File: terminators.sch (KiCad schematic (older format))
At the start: 12 parts

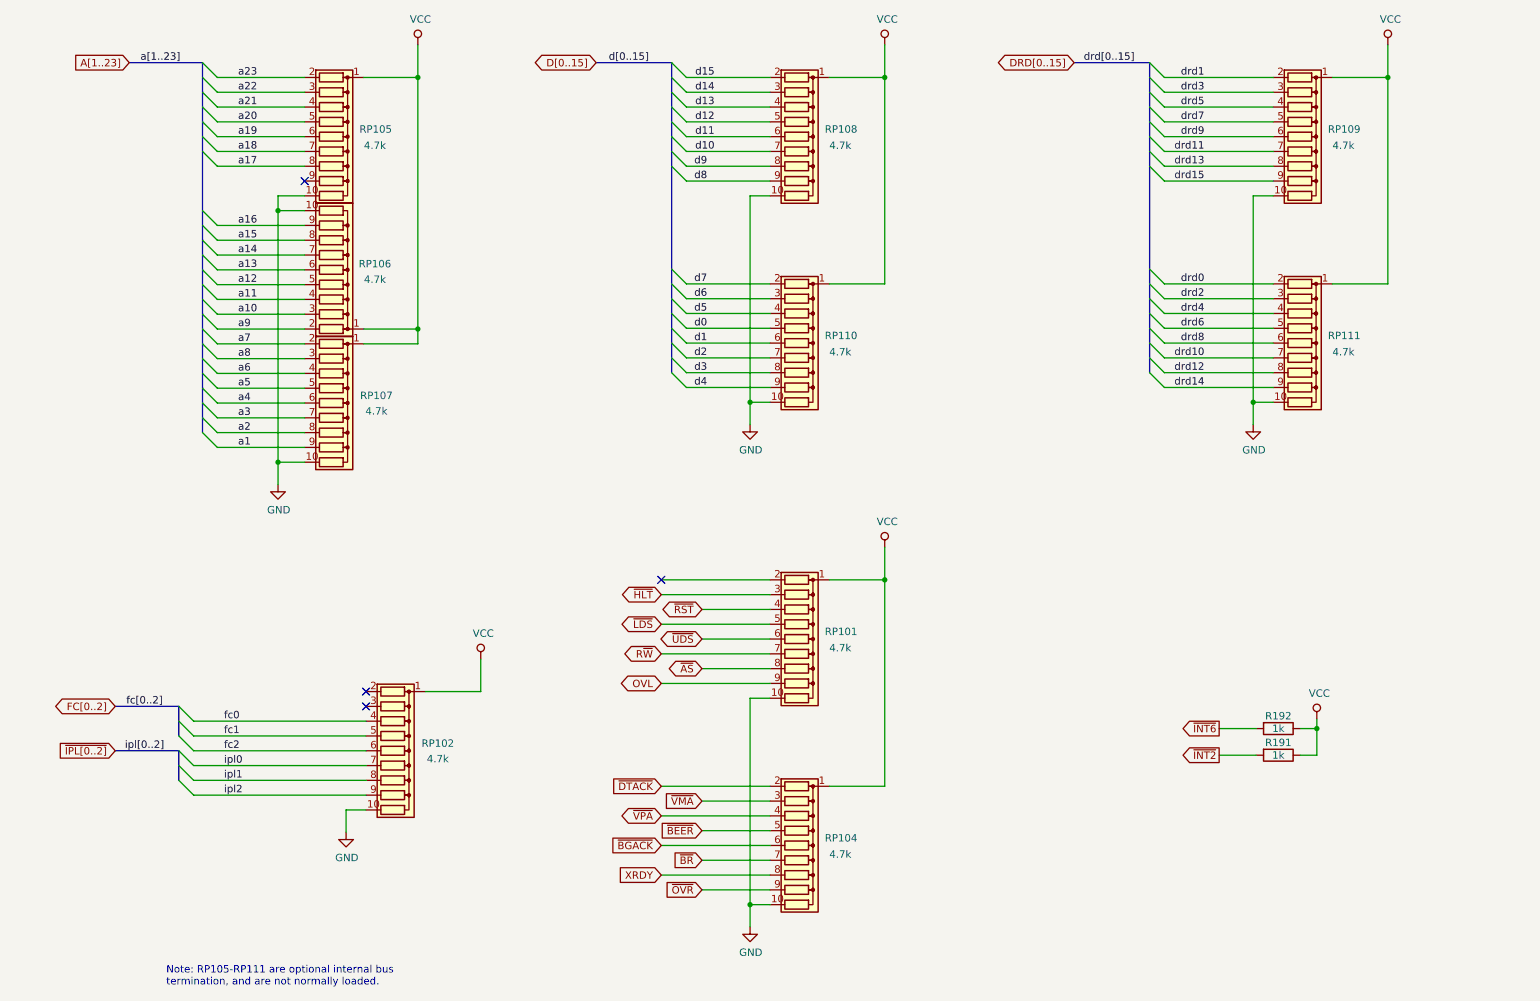
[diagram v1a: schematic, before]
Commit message: Add expansion bus
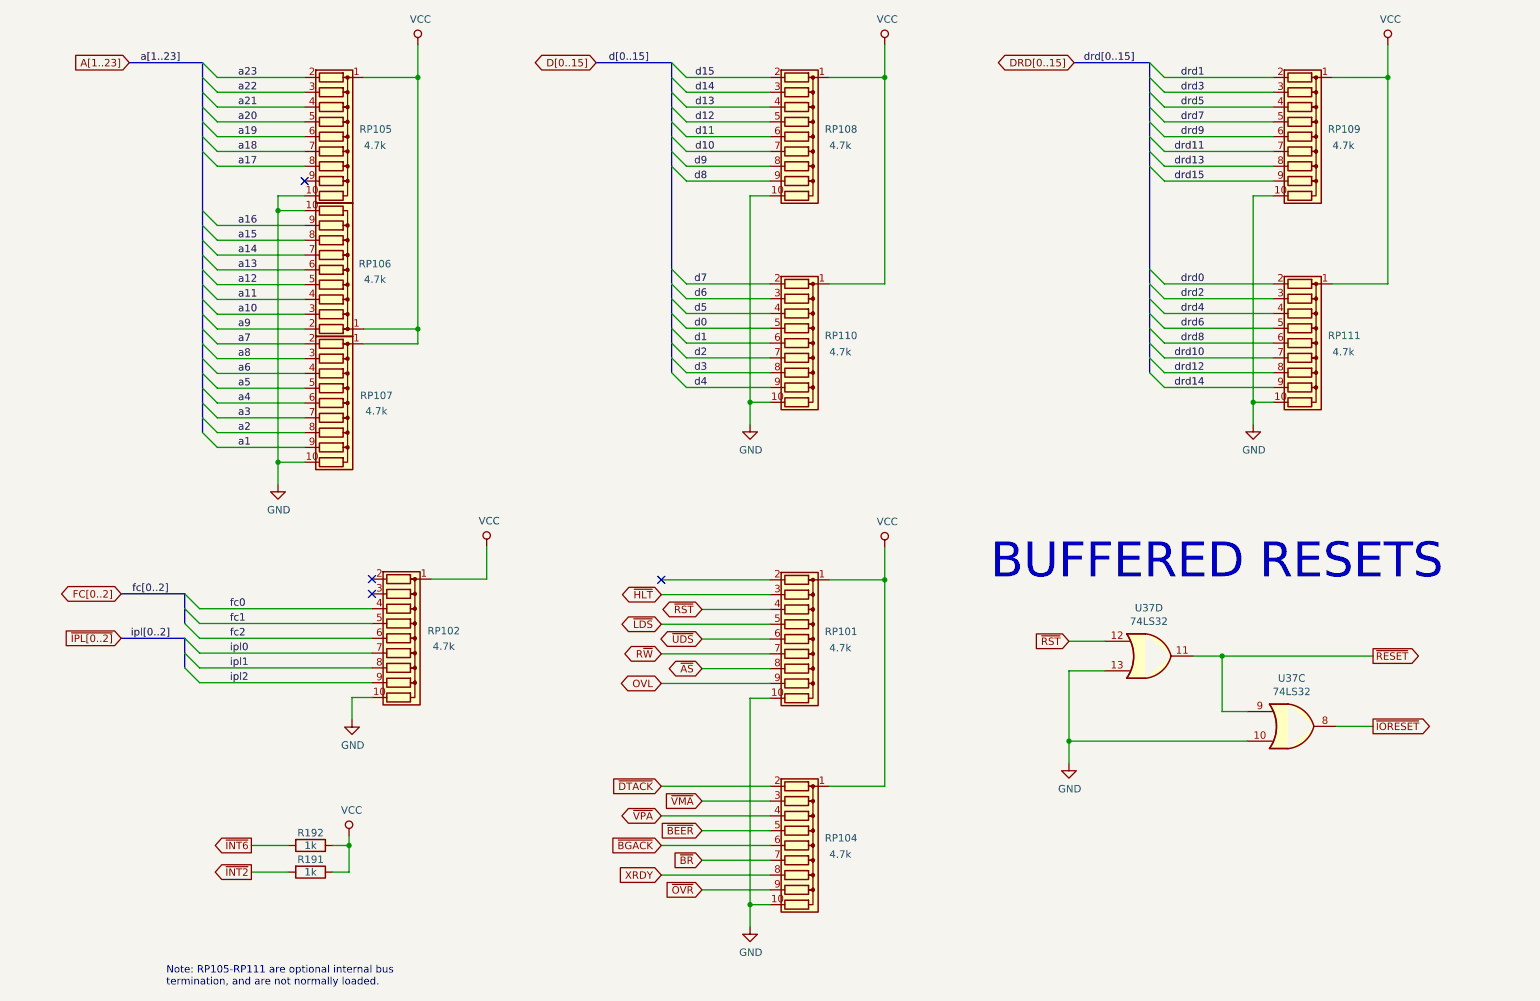
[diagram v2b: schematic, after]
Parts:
- added U37: 74LS32, symbol 74xx:74LS32
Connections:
- net GND: now also U37.10, U37.13
- net ~RST: now also U37.12
- new net ~IORESET: U37.8
- new net ~RESET: U37.11, U37.9
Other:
- note added: "BUFFERED RESETS"
- moved on the sheet: R191, R192, RP102
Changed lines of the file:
@@
 $Descr A4 11693 8268
 encoding utf-8
-Sheet 8 10
+Sheet 8 11
 Title "Rämixx500"
 Date "2019-04-20"
@@
 drd[0..15]
 Wire Wire Line
-	3370 5945 2205 5945
-Wire Wire Line
-	3370 6045 2205 6045
-Wire Wire Line
-	3370 6145 2205 6145
-Wire Wire Line
-	3370 5645 2205 5645
-Wire Wire Line
-	3370 5745 2205 5745
-Wire Wire Line
-	3370 5845 2205 5845
-Entry Wire Line
-	2105 5845 2205 5945
-Entry Wire Line
-	2105 5945 2205 6045
-Entry Wire Line
-	2105 6045 2205 6145
-Entry Wire Line
-	2105 5545 2205 5645
-Entry Wire Line
-	2105 5645 2205 5745
-Entry Wire Line
-	2105 5745 2205 5845
-Text GLabel 1675 5845 0    50   Input ~ 0
+	3410 5185 2245 5185
+Wire Wire Line
+	3410 5285 2245 5285
+Wire Wire Line
+	3410 5385 2245 5385
+Wire Wire Line
+	3410 4885 2245 4885
+Wire Wire Line
+	3410 4985 2245 4985
+Wire Wire Line
+	3410 5085 2245 5085
+Entry Wire Line
+	2145 5085 2245 5185
+Entry Wire Line
+	2145 5185 2245 5285
+Entry Wire Line
+	2145 5285 2245 5385
+Entry Wire Line
+	2145 4785 2245 4885
+Entry Wire Line
+	2145 4885 2245 4985
+Entry Wire Line
+	2145 4985 2245 5085
+Text GLabel 1715 5085 0    50   Input ~ 0
 ~IPL[0..2]
-Text GLabel 1675 5545 0    50   BiDi ~ 0
+Text GLabel 1715 4785 0    50   BiDi ~ 0
 FC[0..2]
-Text Label 1740 5845 0    50   ~ 0
+Text Label 1780 5085 0    50   ~ 0
 ipl[0..2]
-Text Label 1750 5545 0    50   ~ 0
+Text Label 1790 4785 0    50   ~ 0
 fc[0..2]
-Text Label 2410 5945 0    50   ~ 0
+Text Label 2450 5185 0    50   ~ 0
 ipl0
-Text Label 2410 6045 0    50   ~ 0
+Text Label 2450 5285 0    50   ~ 0
 ipl1
-Text Label 2410 6145 0    50   ~ 0
+Text Label 2450 5385 0    50   ~ 0
 ipl2
-Text Label 2410 5645 0    50   ~ 0
+Text Label 2450 4885 0    50   ~ 0
 fc0
-Text Label 2410 5745 0    50   ~ 0
+Text Label 2450 4985 0    50   ~ 0
 fc1
-Text Label 2410 5845 0    50   ~ 0
+Text Label 2450 5085 0    50   ~ 0
 fc2
 $Comp
 L Device:R_Network09 RP102
 U 1 1 5D7152A6
-P 3570 5845
-F 0 "RP102" V 3520 6130 50  0000 C CNN
-F 1 "4.7k" V 3625 6130 50  0000 C CNN
-F 2 "Resistor_THT:R_Array_SIP10" V 4145 5845 50  0001 C CNN
-F 3 "http://www.vishay.com/docs/31509/csc.pdf" H 3570 5845 50  0001 C CNN
-	1    3570 5845
-	0    1    1    0
-$EndComp
-NoConn ~ 3370 5445
-NoConn ~ 3370 5545
-Wire Wire Line
-	4145 5445 3770 5445
+P 3610 5085
+F 0 "RP102" V 3560 5370 50  0000 C CNN
+F 1 "4.7k" V 3665 5370 50  0000 C CNN
+F 2 "Resistor_THT:R_Array_SIP10" V 4185 5085 50  0001 C CNN
+F 3 "http://www.vishay.com/docs/31509/csc.pdf" H 3610 5085 50  0001 C CNN
+	1    3610 5085
+	0    1    1    0
+$EndComp
+NoConn ~ 3410 4685
+NoConn ~ 3410 4785
+Wire Wire Line
+	4185 4685 3810 4685
 $Comp
 L power:VCC #PWR0191
 U 1 1 5D722215
-P 4145 5225
-F 0 "#PWR0191" H 4145 5075 50  0001 C CNN
-F 1 "VCC" H 4162 5398 50  0000 C CNN
-F 2 "" H 4145 5225 50  0001 C CNN
-F 3 "" H 4145 5225 50  0001 C CNN
-	1    4145 5225
-	1    0    0    -1
-$EndComp
-Wire Wire Line
-	4145 5445 4145 5225
-Wire Wire Line
-	3235 6245 3370 6245
+P 4185 4465
+F 0 "#PWR0191" H 4185 4315 50  0001 C CNN
+F 1 "VCC" H 4202 4638 50  0000 C CNN
+F 2 "" H 4185 4465 50  0001 C CNN
+F 3 "" H 4185 4465 50  0001 C CNN
+	1    4185 4465
+	1    0    0    -1
+$EndComp
+Wire Wire Line
+	4185 4685 4185 4465
+Wire Wire Line
+	3275 5485 3410 5485
 $Comp
 L power:GND #PWR0192
 U 1 1 5D728B9B
-P 3235 6395
-F 0 "#PWR0192" H 3235 6145 50  0001 C CNN
-F 1 "GND" H 3240 6222 50  0000 C CNN
-F 2 "" H 3235 6395 50  0001 C CNN
-F 3 "" H 3235 6395 50  0001 C CNN
-	1    3235 6395
-	1    0    0    -1
-$EndComp
-Wire Wire Line
-	3235 6245 3235 6395
+P 3275 5635
+F 0 "#PWR0192" H 3275 5385 50  0001 C CNN
+F 1 "GND" H 3280 5462 50  0000 C CNN
+F 2 "" H 3275 5635 50  0001 C CNN
+F 3 "" H 3275 5635 50  0001 C CNN
+	1    3275 5635
+	1    0    0    -1
+$EndComp
+Wire Wire Line
+	3275 5485 3275 5635
 Wire Bus Line
-	1675 5545 2105 5545
+	1715 4785 2145 4785
 Wire Bus Line
-	1675 5845 2105 5845
-Wire Wire Line
-	9135 5695 9385 5695
+	1715 5085 2145 5085
+Wire Wire Line
+	2595 6485 2845 6485
 $Comp
 L power:VCC #PWR?
 U 1 1 5D73ED87
-P 9795 5630
+P 3255 6420
 AR Path="/5E7E9EC4/5D73ED87" Ref="#PWR?"  Part="1"
 AR Path="/5D6D5EBE/5D73ED87" Ref="#PWR0193"  Part="1"
-F 0 "#PWR0193" H 9795 5480 50  0001 C CNN
-F 1 "VCC" H 9812 5803 50  0000 C CNN
-F 2 "" H 9795 5630 50  0001 C CNN
-F 3 "" H 9795 5630 50  0001 C CNN
-	1    9795 5630
-	1    0    0    -1
-$EndComp
-Wire Wire Line
-	9795 5630 9795 5695
-Wire Wire Line
-	9795 5695 9685 5695
+F 0 "#PWR0193" H 3255 6270 50  0001 C CNN
+F 1 "VCC" H 3272 6593 50  0000 C CNN
+F 2 "" H 3255 6420 50  0001 C CNN
+F 3 "" H 3255 6420 50  0001 C CNN
+	1    3255 6420
+	1    0    0    -1
+$EndComp
+Wire Wire Line
+	3255 6420 3255 6485
+Wire Wire Line
+	3255 6485 3145 6485
 $Comp
 L Device:R E?
 U 1 1 5D73ED8F
-P 9535 5695
+P 2995 6485
 AR Path="/5E7E9EC4/5D73ED8F" Ref="E?"  Part="1"
 AR Path="/5D6D5EBE/5D73ED8F" Ref="R192"  Part="1"
-F 0 "R192" V 9450 5695 50  0000 C CNN
-F 1 "1k" V 9535 5695 50  0000 C CNN
-F 2 "Raemixx500:R_Axial_DIN0309_L9.0mm_D3.2mm_P12.70mm_Horizontal" V 9465 5695 50  0001 C CNN
-F 3 "~" H 9535 5695 50  0001 C CNN
-	1    9535 5695
-	0    1    1    0
-$EndComp
-Wire Wire Line
-	9135 5875 9385 5875
-Wire Wire Line
-	9795 5875 9685 5875
+F 0 "R192" V 2910 6485 50  0000 C CNN
+F 1 "1k" V 2995 6485 50  0000 C CNN
+F 2 "Raemixx500:R_Axial_DIN0309_L9.0mm_D3.2mm_P12.70mm_Horizontal" V 2925 6485 50  0001 C CNN
+F 3 "~" H 2995 6485 50  0001 C CNN
+	1    2995 6485
+	0    1    1    0
+$EndComp
+Wire Wire Line
+	2595 6665 2845 6665
+Wire Wire Line
+	3255 6665 3145 6665
 $Comp
 L Device:R E?
 U 1 1 5D749EFE
-P 9535 5875
+P 2995 6665
 AR Path="/5E7E9EC4/5D749EFE" Ref="E?"  Part="1"
 AR Path="/5D6D5EBE/5D749EFE" Ref="R191"  Part="1"
-F 0 "R191" V 9450 5875 50  0000 C CNN
-F 1 "1k" V 9535 5875 50  0000 C CNN
-F 2 "Raemixx500:R_Axial_DIN0309_L9.0mm_D3.2mm_P12.70mm_Horizontal" V 9465 5875 50  0001 C CNN
-F 3 "~" H 9535 5875 50  0001 C CNN
-	1    9535 5875
-	0    1    1    0
-$EndComp
-Wire Wire Line
-	9795 5875 9795 5695
-Connection ~ 9795 5695
-Text GLabel 9135 5695 0    50   Output ~ 0
+F 0 "R191" V 2910 6665 50  0000 C CNN
+F 1 "1k" V 2995 6665 50  0000 C CNN
+F 2 "Raemixx500:R_Axial_DIN0309_L9.0mm_D3.2mm_P12.70mm_Horizontal" V 2925 6665 50  0001 C CNN
+F 3 "~" H 2995 6665 50  0001 C CNN
+	1    2995 6665
+	0    1    1    0
+$EndComp
+Wire Wire Line
+	3255 6665 3255 6485
+Connection ~ 3255 6485
+Text GLabel 2595 6485 0    50   Output ~ 0
 ~INT6
-Text GLabel 9135 5875 0    50   Output ~ 0
+Text GLabel 2595 6665 0    50   Output ~ 0
 ~INT2
 Wire Wire Line
@@
 Text Notes 2020 7440 0    50   ~ 0
 Note: RP105-RP111 are optional internal bus\ntermination, and are not normally loaded.
+$Comp
+L 74xx:74LS32 U37
+U 4 1 5E9A1FC7
+P 8660 5205
+F 0 "U37" H 8660 5530 50  0000 C CNN
+F 1 "74LS32" H 8660 5439 50  0000 C CNN
+F 2 "" H 8660 5205 50  0001 C CNN
+F 3 "http://www.ti.com/lit/gpn/sn74LS32" H 8660 5205 50  0001 C CNN
+	4    8660 5205
+	1    0    0    -1
+$EndComp
+$Comp
+L 74xx:74LS32 U37
+U 3 1 5E9A2072
+P 9625 5680
+F 0 "U37" H 9625 6005 50  0000 C CNN
+F 1 "74LS32" H 9625 5914 50  0000 C CNN
+F 2 "" H 9625 5680 50  0001 C CNN
+F 3 "http://www.ti.com/lit/gpn/sn74LS32" H 9625 5680 50  0001 C CNN
+	3    9625 5680
+	1    0    0    -1
+$EndComp
+Wire Wire Line
+	8960 5205 9155 5205
+Text GLabel 10175 5205 2    50   Output ~ 0
+~RESET
+Wire Wire Line
+	9155 5205 9155 5580
+Wire Wire Line
+	9155 5580 9325 5580
+Connection ~ 9155 5205
+Wire Wire Line
+	9155 5205 10175 5205
+Wire Wire Line
+	9925 5680 10175 5680
+Text GLabel 10175 5680 2    50   Output ~ 0
+~IORESET
+Wire Wire Line
+	8360 5105 8120 5105
+Text GLabel 8120 5105 0    50   Input ~ 0
+~RST
+Wire Wire Line
+	8360 5305 8120 5305
+Wire Wire Line
+	8120 5305 8120 5780
+Wire Wire Line
+	8120 5780 9325 5780
+$Comp
+L power:GND #PWR?
+U 1 1 5E9C71DF
+P 8120 5930
+F 0 "#PWR?" H 8120 5680 50  0001 C CNN
+F 1 "GND" H 8125 5757 50  0000 C CNN
+F 2 "" H 8120 5930 50  0001 C CNN
+F 3 "" H 8120 5930 50  0001 C CNN
+	1    8120 5930
+	1    0    0    -1
+$EndComp
+Wire Wire Line
+	8120 5780 8120 5930
+Connection ~ 8120 5780
+Text Notes 7590 4705 0    236  ~ 0
+BUFFERED RESETS
 Wire Bus Line
-	2105 5545 2105 5745
+	2145 5085 2145 5285
 Wire Bus Line
-	2105 5845 2105 6045
+	2145 4785 2145 4985
 Wire Bus Line
 	5435 1195 5435 3290

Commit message: Add power & decoupling, not yet complete
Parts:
- U37: footprint (none) -> Package_DIP:DIP-14_W7.62mm_Socket_LongPads
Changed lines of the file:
@@
 $Descr A4 11693 8268
 encoding utf-8
-Sheet 8 11
+Sheet 8 12
 Title "Rämixx500"
 Date "2019-04-20"
@@
 F 0 "U37" H 8660 5530 50  0000 C CNN
 F 1 "74LS32" H 8660 5439 50  0000 C CNN
-F 2 "" H 8660 5205 50  0001 C CNN
+F 2 "Package_DIP:DIP-14_W7.62mm_Socket_LongPads" H 8660 5205 50  0001 C CNN
 F 3 "http://www.ti.com/lit/gpn/sn74LS32" H 8660 5205 50  0001 C CNN
 	4    8660 5205
@@
 F 0 "U37" H 9625 6005 50  0000 C CNN
 F 1 "74LS32" H 9625 5914 50  0000 C CNN
-F 2 "" H 9625 5680 50  0001 C CNN
+F 2 "Package_DIP:DIP-14_W7.62mm_Socket_LongPads" H 9625 5680 50  0001 C CNN
 F 3 "http://www.ti.com/lit/gpn/sn74LS32" H 9625 5680 50  0001 C CNN
 	3    9625 5680
@@
 	8120 5780 9325 5780
 $Comp
-L power:GND #PWR?
+L power:GND #PWR0226
 U 1 1 5E9C71DF
 P 8120 5930
-F 0 "#PWR?" H 8120 5680 50  0001 C CNN
+F 0 "#PWR0226" H 8120 5680 50  0001 C CNN
 F 1 "GND" H 8125 5757 50  0000 C CNN
 F 2 "" H 8120 5930 50  0001 C CNN
